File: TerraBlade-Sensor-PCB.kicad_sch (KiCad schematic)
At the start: 25 parts, among them SW1 TS-1187A-B-A-B, U1 XIAO-ESP32-C3-SMD, U2 2.1MHz

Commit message: PCB Design
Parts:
- removed BLADE1: SensorBlade, SensorBlade:SensorBlade_Tenon, symbol SensorBlade:SensorBlade
- removed H3, H4: 2.54-1*4P母, Custom:HDR-TH_4P-P2.54-V-F, symbol Custom:2.54-1*4P母
- removed H7, H8: PZ254V-11-04P_C2691448, Custom:HDR-TH_4P-P2.54-V-M, symbol Custom:PZ254V-11-04P_C2691448
- added PAD5, PAD6: BladePad, Custom:BladePad_SMD, symbol Custom:BladePad
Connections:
- new net PROBE_BACK: PAD6.1
- new net PROBE_FRONT: PAD5.1
- no-connect marks 31 -> 21
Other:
- moved on the sheet: H1, H2, H5, H6, PAD3, PAD4

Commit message: PCB Layout
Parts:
- removed PAD3: PowerPad+, Custom:BladePad_SMD, symbol Custom:BladePad
- removed PAD4: PowerPad-, Custom:BladePad_SMD, symbol Custom:BladePad
- added CN3: PowerPad+, Custom:TESTPOINT-SMD_BD2.0-D1.0-Custom, symbol Custom:PG1000-01-010P
- added CN4: PowerPad-, Custom:TESTPOINT-SMD_BD2.0-D1.0-Custom, symbol Custom:PG1000-01-010P
- C1: Supplier Part (none) -> C476766
- R2, R5: Supplier Part (none) -> C17414
- SW1: Supplier Part (none) -> C318884
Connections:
- net POWER_PAD_+: now reaches H5.1
- net POWER_PAD_+: now also CN3.1
- net POWER_PAD_-: now reaches H5.2
- net POWER_PAD_-: now also H5.3, H5.4, H6.1, H6.2, H6.3, H6.4, CN4.1
- no-connect marks 21 -> 15
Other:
- moved on the sheet: H5, H6

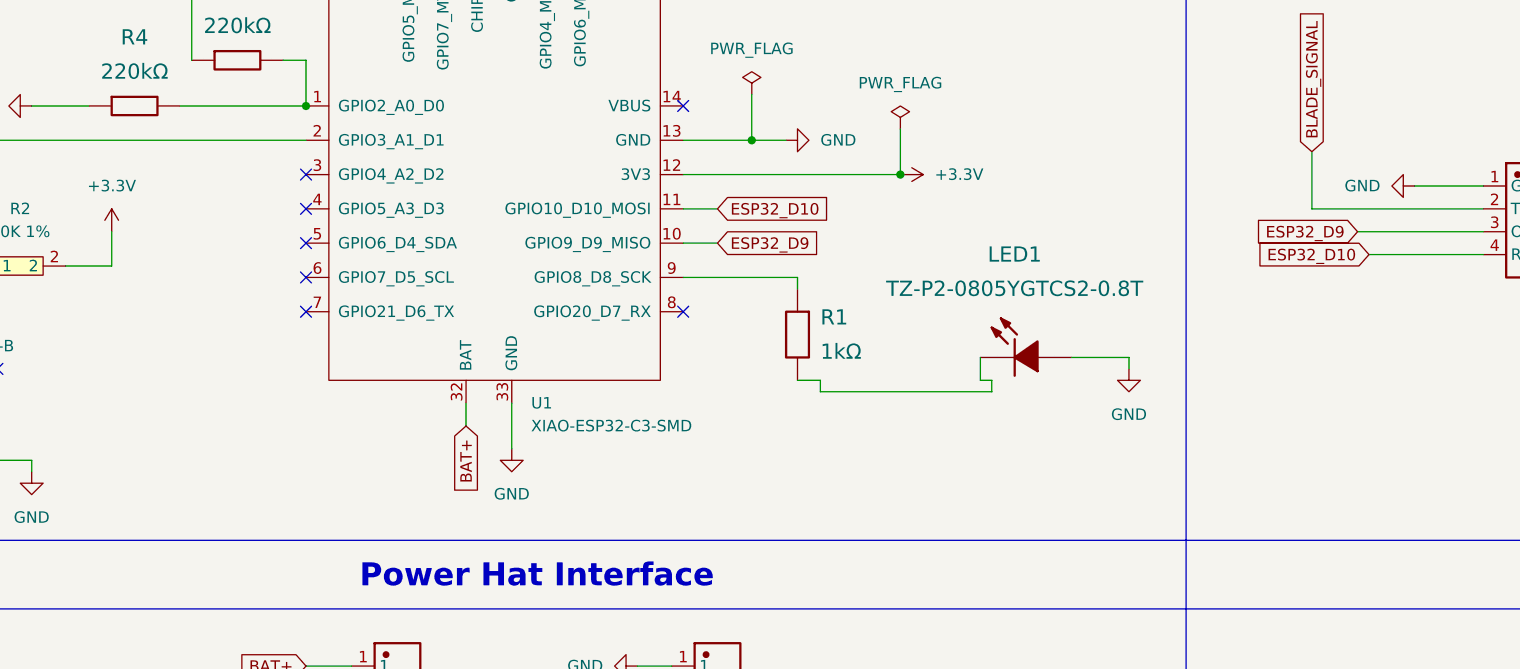
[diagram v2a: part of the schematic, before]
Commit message: Remap Digital Pins (Don't use strapping pins) / Increase size of the mortise tenon slot
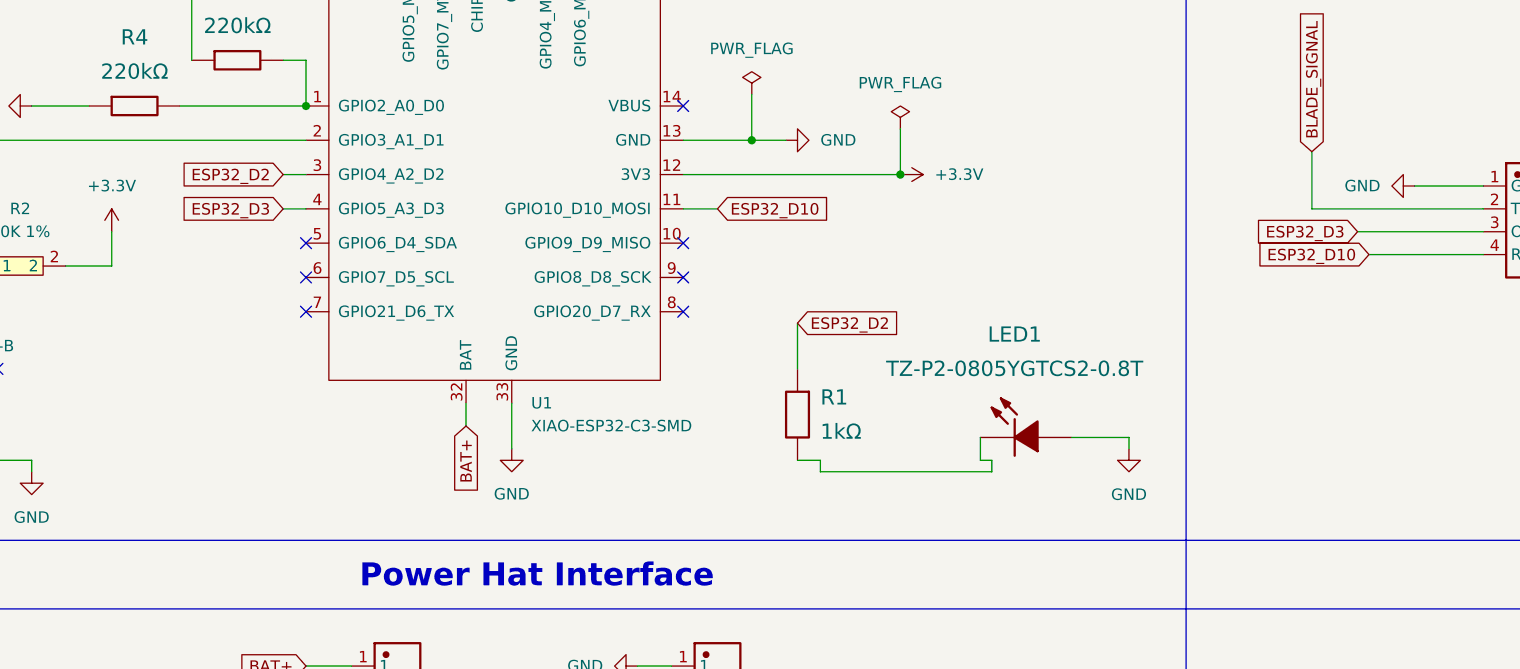
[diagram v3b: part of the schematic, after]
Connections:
- net ESP32_D2: now reaches U1.3 (GPIO4_A2_D2)
- net ESP32_D2: now also R1.1
- net ESP32_D3: now reaches U1.4 (GPIO5_A3_D3)
- net ESP32_D3: now also U2.3 (OUT)
- net at U1.9 (GPIO8_D8_SCK): no longer R1.1
- net ESP32_D9: no longer names the net of U1.10 (GPIO9_D9_MISO)
- net ESP32_D9: no longer U2.3 (OUT)
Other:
- moved on the sheet: LED1, R1
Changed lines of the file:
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@@
 		(title "TerraBlade Soil Moisture Sensor")
 		(date "2026-04-04")
+		(rev "1")
 		(company "BJD Solutions")
 	)
@@
 	)
 	(no_connect
-		(at 62.23 62.23)
+		(at 73.66 35.56)
 	)
 	(no_connect
-		(at 73.66 35.56)
+		(at 104.14 73.66)
 	)
 	(no_connect
@@
 	)
 	(no_connect
-		(at 62.23 66.04)
+		(at 104.14 69.85)
 	)
 	(no_connect
@@
 	(wire
 		(pts
-			(xy 119.38 85.09) (xy 116.84 85.09)
+			(xy 119.38 93.98) (xy 116.84 93.98)
 		)
 		(stroke
@@
 	(wire
 		(pts
-			(xy 119.38 86.36) (xy 138.43 86.36)
+			(xy 119.38 95.25) (xy 138.43 95.25)
 		)
 		(stroke
@@
 	(wire
 		(pts
-			(xy 137.16 85.09) (xy 137.16 82.55)
+			(xy 137.16 93.98) (xy 137.16 91.44)
 		)
 		(stroke
@@
 	(wire
 		(pts
-			(xy 104.14 69.85) (xy 107.95 69.85)
-		)
-		(stroke
-			(width 0)
-			(type default)
-		)
-	)
-	(wire
-		(pts
-			(xy 153.67 82.55) (xy 153.67 83.82)
+			(xy 153.67 91.44) (xy 153.67 92.71)
 		)
 		(stroke
@@
 	(wire
 		(pts
-			(xy 119.38 85.09) (xy 119.38 86.36)
+			(xy 119.38 93.98) (xy 119.38 95.25)
 		)
 		(stroke
@@
 	(wire
 		(pts
-			(xy 138.43 85.09) (xy 137.16 85.09)
+			(xy 138.43 93.98) (xy 137.16 93.98)
 		)
 		(stroke
@@
 	(wire
 		(pts
+			(xy 59.69 62.23) (xy 62.23 62.23)
+		)
+		(stroke
+			(width 0)
+			(type default)
+		)
+	)
+	(wire
+		(pts
 			(xy 104.14 58.42) (xy 111.76 58.42)
 		)
@@
 	(wire
 		(pts
-			(xy 138.43 86.36) (xy 138.43 85.09)
+			(xy 138.43 95.25) (xy 138.43 93.98)
 		)
 		(stroke
@@
 	(wire
 		(pts
-			(xy 147.32 82.55) (xy 153.67 82.55)
+			(xy 59.69 66.04) (xy 62.23 66.04)
 		)
 		(stroke
@@
 	(wire
 		(pts
-			(xy 134.62 154.94) (xy 127 154.94)
+			(xy 147.32 91.44) (xy 153.67 91.44)
 		)
 		(stroke
@@
 	(wire
 		(pts
-			(xy 31.75 54.61) (xy 38.1 54.61)
+			(xy 134.62 154.94) (xy 127 154.94)
 		)
 		(stroke
@@
 	(wire
 		(pts
-			(xy 134.62 148.59) (xy 134.62 151.13)
+			(xy 31.75 54.61) (xy 38.1 54.61)
 		)
 		(stroke
@@
 	(wire
 		(pts
-			(xy 99.06 116.84) (xy 102.87 116.84)
+			(xy 134.62 148.59) (xy 134.62 151.13)
 		)
 		(stroke
@@
 	(wire
 		(pts
-			(xy 104.14 73.66) (xy 116.84 73.66)
+			(xy 99.06 116.84) (xy 102.87 116.84)
 		)
 		(stroke
@@
 	(wire
 		(pts
-			(xy 116.84 73.66) (xy 116.84 74.93)
+			(xy 116.84 78.74) (xy 116.84 83.82)
 		)
 		(stroke
@@
 		)
 	)
+	(global_label "ESP32_D2"
+		(shape input)
+		(at 59.69 62.23 180)
+		(fields_autoplaced yes)
+		(effects
+			(font
+				(size 1.27 1.27)
+			)
+			(justify right)
+		)
+		(property "Intersheetrefs" "${INTERSHEET_REFS}"
+			(at 47.2102 62.23 0)
+			(effects
+				(font
+					(size 1.27 1.27)
+				)
+				(justify right)
+				(hide yes)
+			)
+		)
+	)
 	(global_label "BAT+"
 		(shape input)
@@
 		)
 	)
-	(global_label "ESP32_D9"
+	(global_label "ESP32_D3"
 		(shape input)
 		(at 179.07 68.58 180)
@@
 		)
 	)
+	(global_label "ESP32_D2"
+		(shape input)
+		(at 116.84 78.74 0)
+		(fields_autoplaced yes)
+		(effects
+			(font
+				(size 1.27 1.27)
+			)
+			(justify left)
+		)
+		(property "Intersheetrefs" "${INTERSHEET_REFS}"
+			(at 129.3198 78.74 0)
+			(effects
+				(font
+					(size 1.27 1.27)
+				)
+				(justify left)
+				(hide yes)
+			)
+		)
+	)
 	(global_label "BAT+"
 		(shape input)
@@
 		)
 	)
-	(global_label "ESP32_D9"
+	(global_label "ESP32_D3"
 		(shape input)
-		(at 107.95 69.85 0)
+		(at 59.69 66.04 180)
 		(fields_autoplaced yes)
 		(effects
@@
 				(size 1.27 1.27)
 			)
-			(justify left)
+			(justify right)
 		)
 		(property "Intersheetrefs" "${INTERSHEET_REFS}"
-			(at 120.4298 69.85 0)
+			(at 47.2102 66.04 0)
 			(effects
 				(font
 					(size 1.27 1.27)
 				)
-				(justify left)
+				(justify right)
 				(hide yes)
 			)
@@
 	(symbol
 		(lib_id "Custom:FRC0805J102_TS")
-		(at 116.84 80.01 270)
+		(at 116.84 88.9 270)
 		(unit 1)
 		(exclude_from_sim no)
@@
 		(fields_autoplaced yes)
 		(property "Reference" "R1"
-			(at 119.38 78.1049 90)
+			(at 119.38 86.9949 90)
 			(effects
 				(font
@@
 		)
 		(property "Value" "1kΩ"
-			(at 119.38 81.9149 90)
+			(at 119.38 90.8049 90)
 			(effects
 				(font
@@
 		)
 		(property "Footprint" "Custom:R0805"
-			(at 116.84 80.01 0)
+			(at 116.84 88.9 0)
 			(effects
 				(font
@@
 		)
 		(property "Datasheet" "https://www.lcsc.com/product-detail/C2907295.html"
-			(at 116.84 80.01 0)
+			(at 116.84 88.9 0)
 			(effects
 				(font
@@
 		)
 		(property "Description" ""
-			(at 116.84 80.01 0)
+			(at 116.84 88.9 0)
 			(effects
 				(font
@@
 		)
 		(property "Manufacturer Part" "FRC0805J102 TS"
-			(at 116.84 80.01 0)
+			(at 116.84 88.9 0)
 			(effects
 				(font
@@
 		)
 		(property "Manufacturer" "FOJAN(富捷)"
-			(at 116.84 80.01 0)
+			(at 116.84 88.9 0)
 			(effects
 				(font
@@
 		)
 		(property "Supplier Part" "C2907295"
-			(at 116.84 80.01 0)
+			(at 116.84 88.9 0)
 			(effects
 				(font
@@
 		)
 		(property "Supplier" "LCSC"
-			(at 116.84 80.01 0)
+			(at 116.84 88.9 0)
 			(effects
 				(font
@@
 	(symbol
 		(lib_id "Custom:TZ-P2-0805YGTCS2-0.8T")
-		(at 142.24 82.55 0)
+		(at 142.24 91.44 0)
 		(unit 1)
 		(exclude_from_sim no)
@@
 		(fields_autoplaced yes)
 		(property "Reference" "LED1"
-			(at 140.97 71.12 0)
+			(at 140.97 80.01 0)
 			(effects
 				(font
@@
 		)
 		(property "Value" "TZ-P2-0805YGTCS2-0.8T"
-			(at 140.97 74.93 0)
+			(at 140.97 83.82 0)
 			(effects
 				(font
@@
 		)
 		(property "Footprint" "Custom:LED0805-R-RD_GREEN"
-			(at 142.24 82.55 0)
+			(at 142.24 91.44 0)
 			(effects
 				(font
@@
 		)
 		(property "Datasheet" "https://www.lcsc.com/product-detail/C688885.html"
-			(at 142.24 82.55 0)
+			(at 142.24 91.44 0)
 			(effects
 				(font
@@
 		)
 		(property "Description" ""
-			(at 142.24 82.55 0)
+			(at 142.24 91.44 0)
 			(effects
 				(font
@@
 		)
 		(property "Manufacturer Part" "TZ-P2-0805YGTCS2-0.8T"
-			(at 142.24 82.55 0)
+			(at 142.24 91.44 0)
 			(effects
 				(font
@@
 		)
 		(property "Manufacturer" "TUOZHAN(拓展光电)"
-			(at 142.24 82.55 0)
+			(at 142.24 91.44 0)
 			(effects
 				(font
@@
 		)
 		(property "Supplier Part" "C688885"
-			(at 142.24 82.55 0)
+			(at 142.24 91.44 0)
 			(effects
 				(font
@@
 		)
 		(property "Supplier" "LCSC"
-			(at 142.24 82.55 0)
+			(at 142.24 91.44 0)
 			(effects
 				(font
@@
 	(symbol
 		(lib_id "power:GND")
-		(at 153.67 83.82 0)
+		(at 153.67 92.71 0)
 		(unit 1)
 		(exclude_from_sim no)
@@
 		(fields_autoplaced yes)
 		(property "Reference" "#PWR01"
-			(at 153.67 90.17 0)
+			(at 153.67 99.06 0)
 			(effects
 				(font
@@
 		)
 		(property "Value" "GND"
-			(at 153.67 88.9 0)
+			(at 153.67 97.79 0)
 			(effects
 				(font
@@
 		)
 		(property "Footprint" ""
-			(at 153.67 83.82 0)
+			(at 153.67 92.71 0)
 			(effects
 				(font
@@
 		)
 		(property "Datasheet" ""
-			(at 153.67 83.82 0)
+			(at 153.67 92.71 0)
 			(effects
 				(font
@@
 		)
 		(property "Description" "Power symbol creates a global label with name \"GND\" , ground"
-			(at 153.67 83.82 0)
+			(at 153.67 92.71 0)
 			(effects
 				(font
